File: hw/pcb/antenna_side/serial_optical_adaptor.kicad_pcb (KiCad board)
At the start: 2 copper layers, 40 x 58.7 mm, 28 parts, among them IC1 ATMEGA168PA-A, P1 CONN_02X03, P2 Battery, P3 CONN_01X01, P4 CONN_01X04, U1 LM393, U2 LP3984, U3 ADG3300

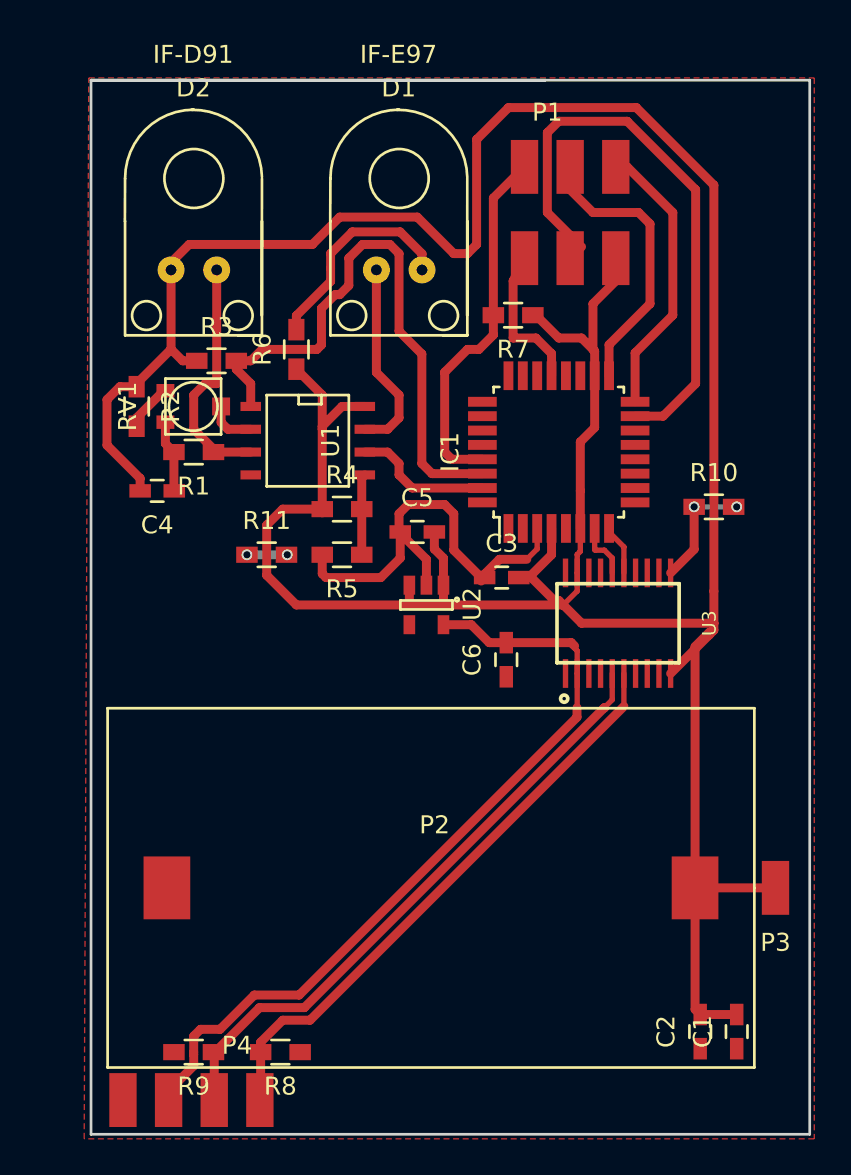
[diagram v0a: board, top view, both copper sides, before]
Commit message: 
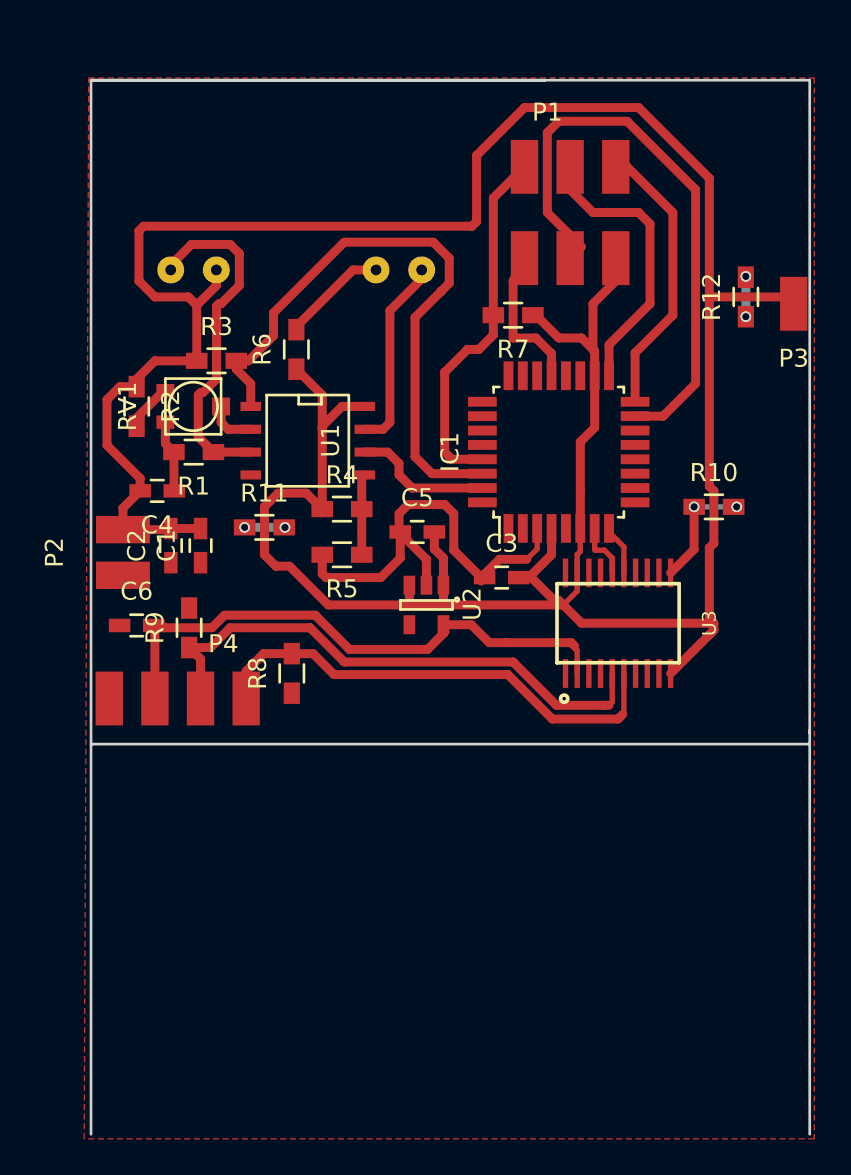
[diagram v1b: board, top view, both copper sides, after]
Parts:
- added R12: R, Resistors_SMD:R_0603_HandSoldering, F.Cu at (120.9, 37.7)
- D1, D2: moved to B.Cu
- P2: footprint hw:SMTU2032-1 -> antenna_side:Batt
- moved C1 40.3 mm to (90.6, 51.6)
- moved C2 40.0 mm to (88.9, 51.6)
- moved P3 32.5 mm to (123.6, 40.6)
- moved P2 27.1 mm to (83.7, 51.9), turned to 270 degrees
- moved R9 23.6 mm to (89.9, 56.1), turned to 90 degrees
- moved P4 22.4 mm to (91.8, 57.5)
- moved R8 21.1 mm to (95.6, 58.7), turned to 90 degrees
- moved C6 20.7 mm to (87.0, 56.0), turned to 0 degrees
- moved R11 1.53 mm to (94.1, 50.5)
- turned D1 to 0 degrees
- turned D2 to 0 degrees
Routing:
- net /Vrffe: track 44.7 -> 32.7 mm
- net /VCC: track 195.7 -> 185.3 mm
- net Net-(D2-Pad1): track 13.6 -> 20.1 mm
- net Net-(D1-Pad1): track 12.0 -> 5.91 mm
- net /RFFE_SCLK: track 33.0 -> 28.6 mm
- net /RFFE_SDATA: track 34.4 -> 30.6 mm
- net /GND: track 46.8 -> 49.1 mm, vias 4 -> 6
- net /RX: track 32.9 -> 34.8 mm
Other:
- outline, holes or cut-outs redrawn
